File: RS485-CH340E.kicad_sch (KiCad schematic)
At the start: 14 parts, among them J1 USB_A, J2 Conn_01x04_Pin, J3 Conn_02x04_Odd_Even, U1 NCP1117-3.3_SOT223, U2 SP3485CN, U3 CH340X

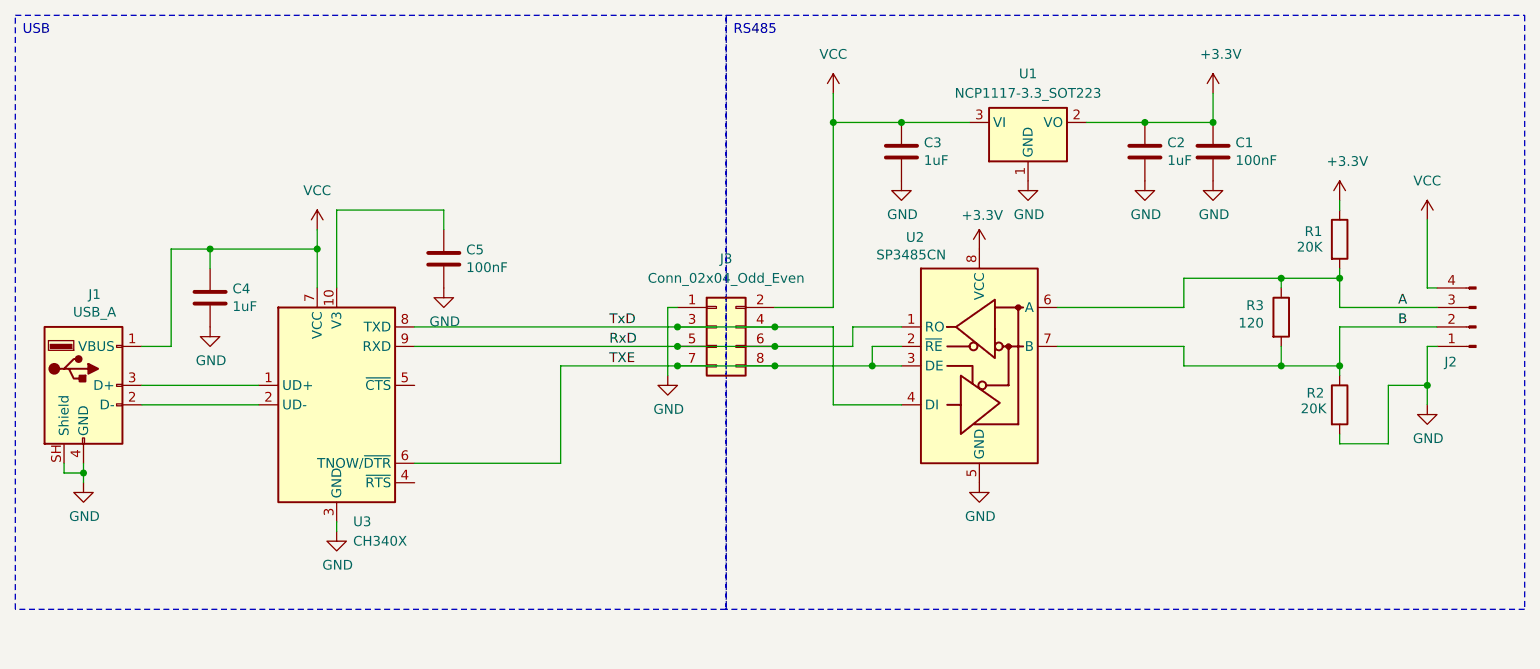
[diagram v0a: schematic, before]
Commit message: Remove 3.3V LDO voltage regulator (use ch340 built-in LDO) Run rs485 transceiver at 5V Make design easier to hand solder
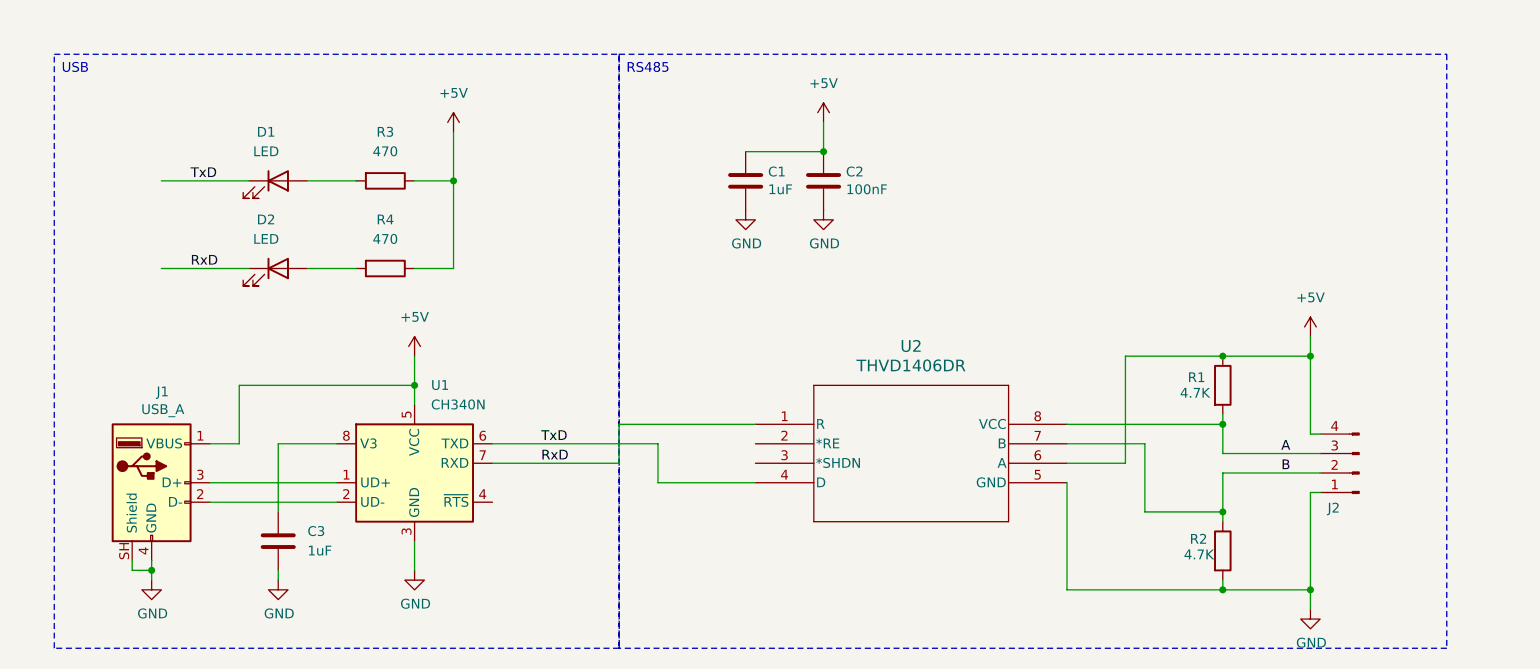
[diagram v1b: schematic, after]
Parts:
- removed C1, C5: 100nF, Capacitor_SMD:C_0603_1608Metric, symbol Device:C
- removed C4: 1uF, Capacitor_SMD:C_0603_1608Metric, symbol Device:C
- removed J3: Conn_02x04_Odd_Even, Connector_PinHeader_1.27mm:PinHeader_2x04_P1.27mm_Vertical, symbol Connector_Generic:Conn_02x04_Odd_Even
- removed U1: NCP1117-3.3_SOT223, Package_TO_SOT_SMD:SOT-23, symbol Regulator_Linear:NCP1117-3.3_SOT223
- removed U2: SP3485CN, Package_SO:SOIC-8_3.9x4.9mm_P1.27mm, symbol Interface_UART:SP3485CN
- removed U3: CH340X, Package_SO:MSOP-10_3x3mm_P0.5mm, symbol Interface_USB:CH340X
- added C3: 1uF, Capacitor_SMD:C_0603_1608Metric_Pad1.08x0.95mm_HandSolder, symbol Device:C
- added D1, D2: LED, LED_SMD:LED_0603_1608Metric_Pad1.05x0.95mm_HandSolder, symbol Device:LED
- added R4: 470, Resistor_SMD:R_0603_1608Metric_Pad0.98x0.95mm_HandSolder, symbol Device:R
- added U1: CH340N, Package_SO:JEITA_SOIC-8_3.9x4.9mm_P1.27mm, symbol Interface_USB:CH340N
- added U2: THVD1406DR, Package_SO:SOIC-8_5.3x6.2mm_P1.27mm, symbol TI tvhd1406:THVD1406DR
- C2: renamed from C3; value 1uF -> 100nF
- R1, R2: value 20K -> 4.7K
- R3: value 120 -> 470; footprint Resistor_SMD:R_0603_1608Metric -> Resistor_SMD:R_0603_1608Metric_Pad0.98x0.95mm_HandSolder
- renumbered C2 to C1
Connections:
- net VCC is gone; now on net +5V: C2.1, J1.1 (VBUS), J2.4 (Pin_4)
- net A: now also U2.8 (VCC); no longer R3.1
- net B: now also U2.7 (B); no longer R3.2
- net GND: now also C3.2, U1.3 (GND), U2.5 (GND)
- net RxD: now also D2.1 (K), U1.7 (RXD), U2.1 (R)
- net TxD: now also D1.1 (K), U1.6 (TXD), U2.4 (D)
- net at J1.2 (D-): now also U1.2 (UD-)
- net at J1.3 (D+): now also U1.1 (UD+)
- net +3.3V renamed +5V
- net +5V: now also R3.1, R4.1, U1.5 (VCC), U2.6 (A)
- new net: D1.2 (A), R3.2
- new net: D2.2 (A), R4.2
- new net: C3.1, U1.8 (V3)
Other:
- moved on the sheet: C1, C2, J2, R1, R2
